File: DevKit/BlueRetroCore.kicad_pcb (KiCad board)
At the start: 4 copper layers, 85 x 56 mm, 108 parts, among them J1 USB_C_Receptacle_USB2.0, J2 Conn_02x06, J3 Micro_SD_Card, J4 Conn_01x03, J5 DB25_Female_MountingHoles, J6 Conn_02x13, J7 Conn_02x07, Q1 BSS138, Q2 BSS138, Q3 S8050, Q4 S8050, Q5 S8050, SW1 BOOT, SW2 EN, U1 ESP32-WROOM, U10 TPD6F003, U11 TPD6F003, U12 TPD6F003, U13 TPD6F003, U2 FT2232HL, U3 STL6N3LLH6, U4 TCPP01-M12, U5 M93C46, U6 ECMF02-2AMX6, U7 TPD6F003, U8 AP7361C-33E, U9 AP7361C-33E, Y1 12MHz

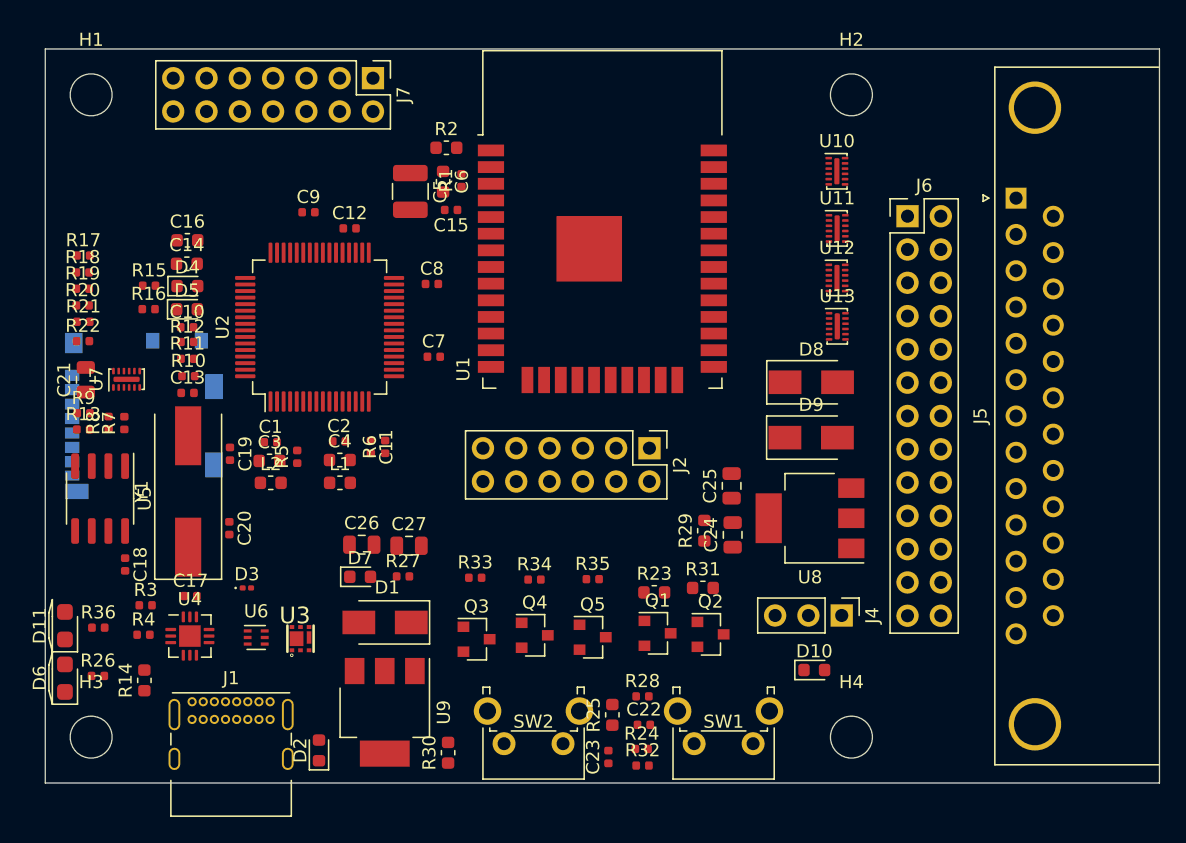
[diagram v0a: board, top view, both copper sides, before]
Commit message: Add cutout for ESP32 antenna
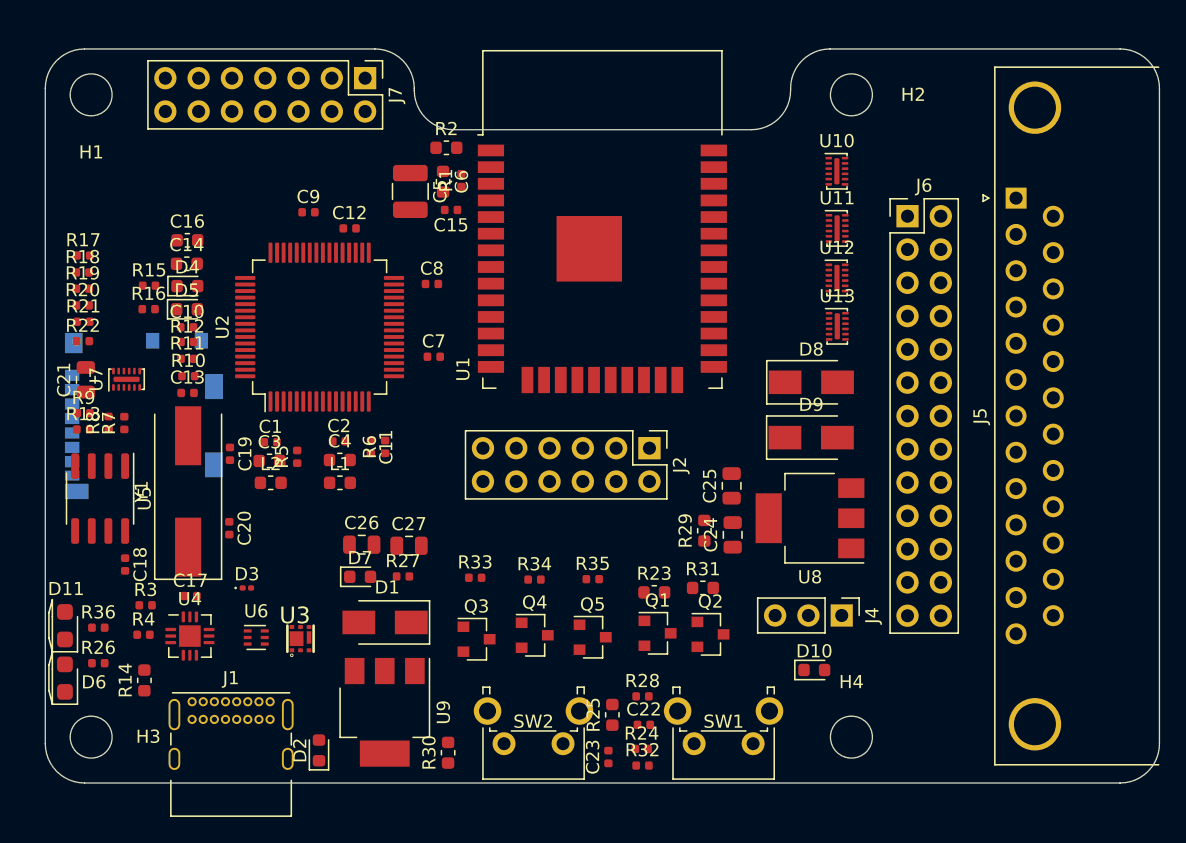
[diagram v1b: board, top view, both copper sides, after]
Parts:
- moved R26 0.97 mm to (-38.5, 18.9)
- moved J7 0.60 mm to (-18.1, -25.8)
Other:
- outline, holes or cut-outs redrawn
